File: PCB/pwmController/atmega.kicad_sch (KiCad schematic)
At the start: 11 parts, among them U201 HEADER_3x2, U202 ATmega328-A, Y201 Crystal_GND2

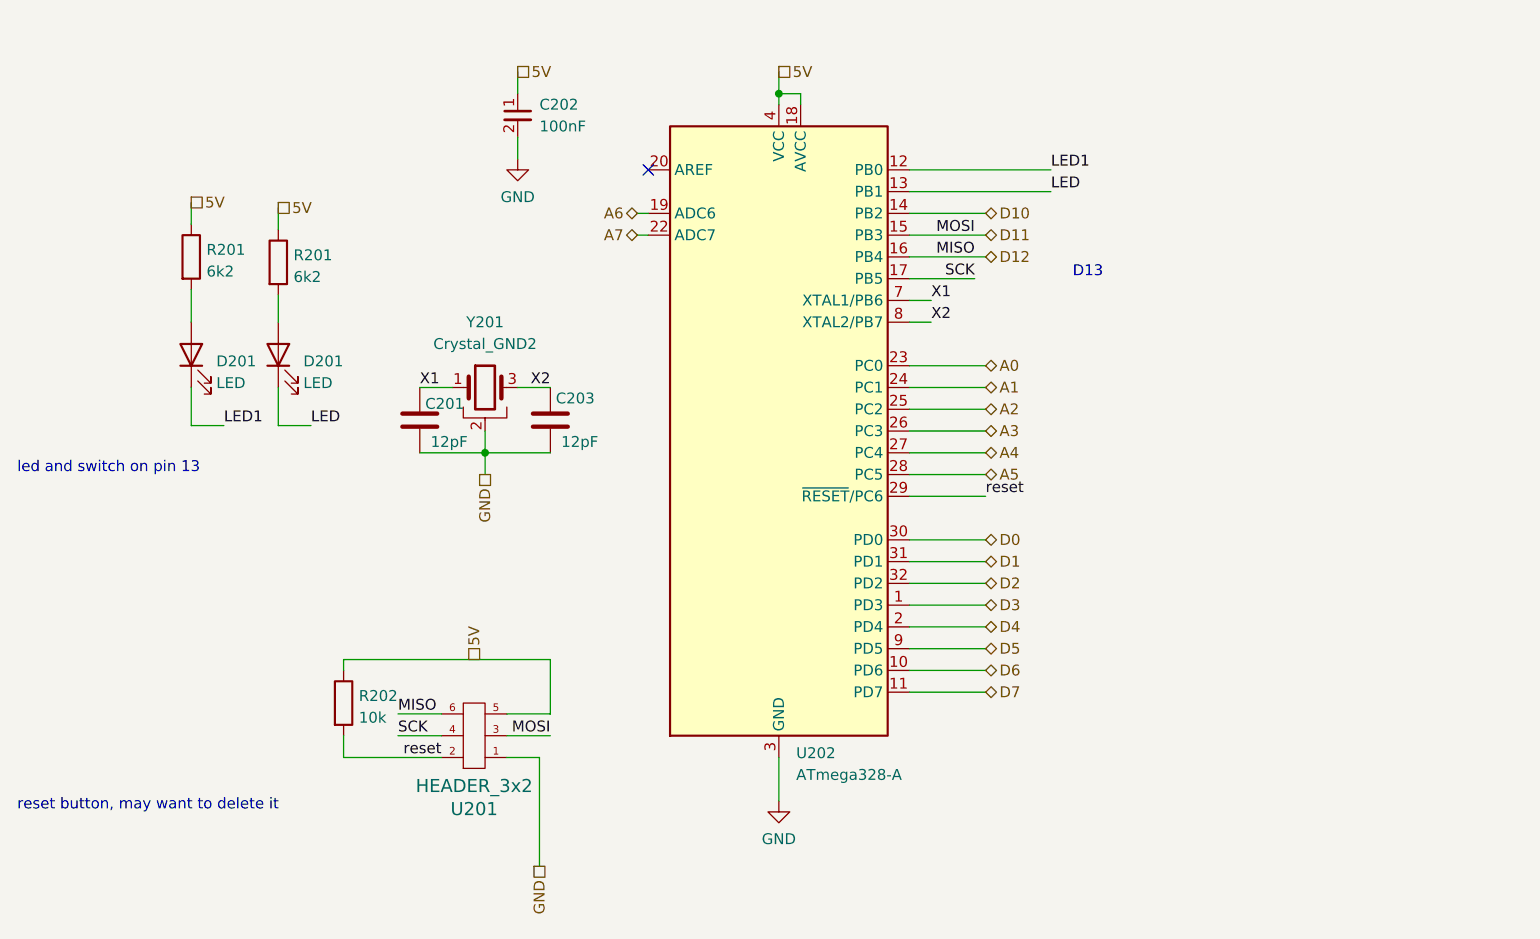
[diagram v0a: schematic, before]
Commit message: added some board files and Xnet block unit binary
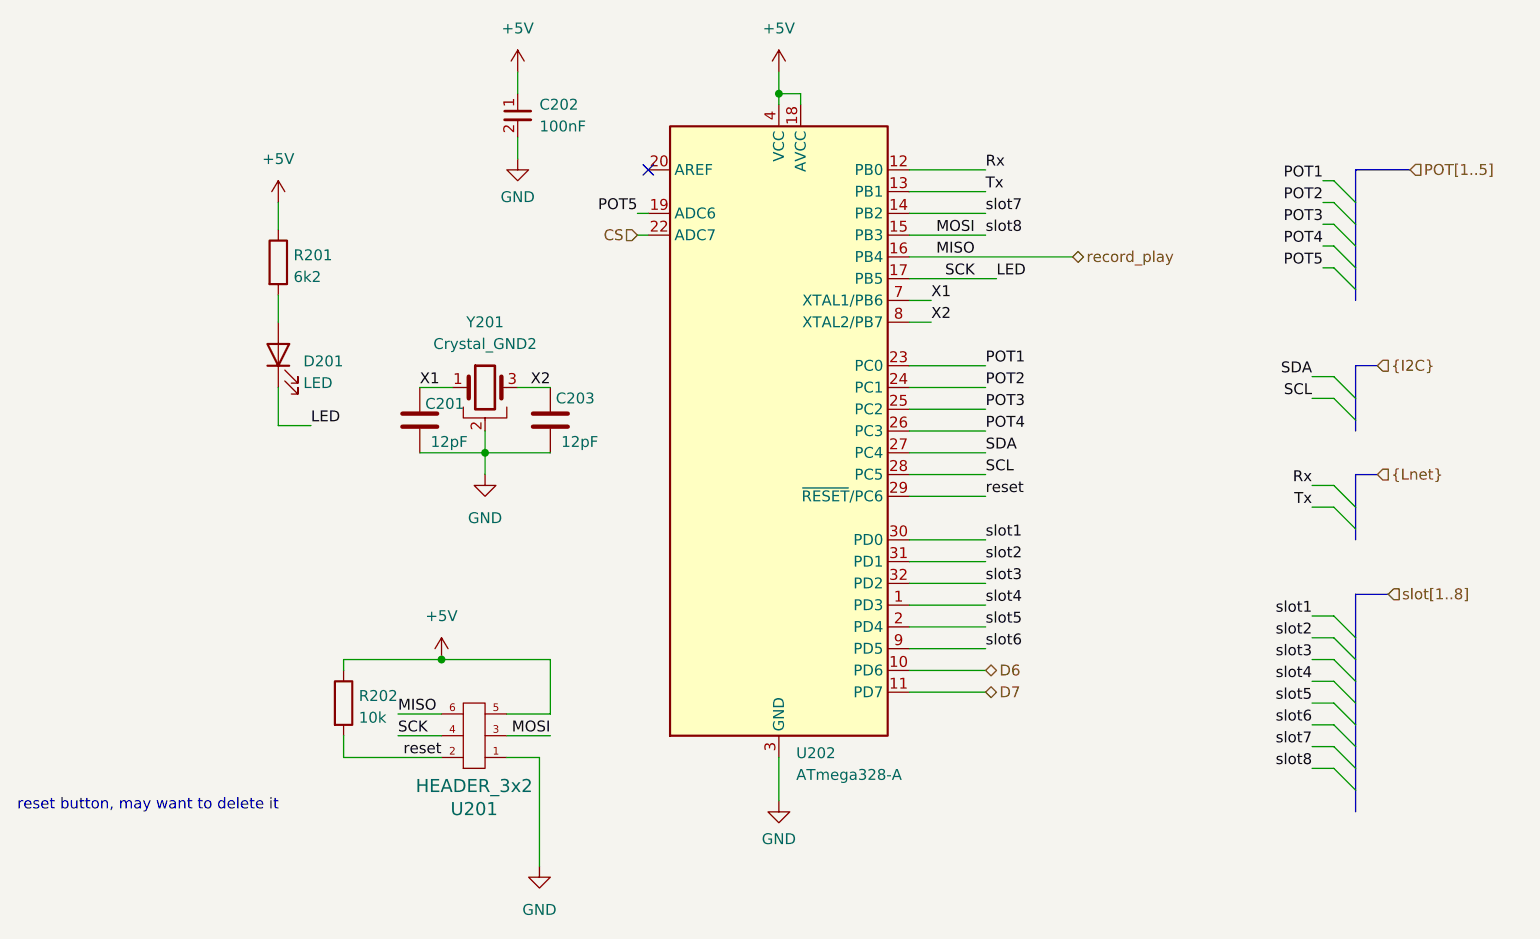
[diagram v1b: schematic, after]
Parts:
- removed D201: LED, LED_THT:LED_D3.0mm, symbol Device:LED
- removed R201: 6k2, Resistor_SMD:R_0603_1608Metric_Pad0.98x0.95mm_HandSolder, symbol Device:R
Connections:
- net SCK is gone; now on net LED: U201.4, U202.17 (PB5)
- net LED: no longer U202.13 (PB1)
- net 5V renamed +5V
- net A0 renamed POT1
- net A1 renamed POT2
- net A2 renamed POT3
- net A3 renamed POT4
- net A4 renamed SDA
- net A5 renamed SCL
- net A6 renamed POT5
- net A7 renamed CS
- net D0 renamed slot1
- net D1 renamed slot2
- net D10 renamed slot7
- net D11 renamed MOSI
- net D12 renamed record_play
- net D2 renamed slot3
- net D3 renamed slot4
- net D4 renamed slot5
- net D5 renamed slot6
- net LED1 renamed Rx
- new net Tx: U202.13 (PB1)
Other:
- note removed: "D13"
- note removed: "led and switch on pin 13"
